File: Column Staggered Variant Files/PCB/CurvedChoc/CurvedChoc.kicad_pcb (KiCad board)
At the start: 2 copper layers, 118.9 x 178.7 mm, 54 parts, among them SW1 2-Pos, SW10 Switch, SW11 Switch, SW12 Switch, SW13 Switch, SW14 Switch, SW15 Switch, SW16 Switch, SW17 Switch, SW18 REsw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

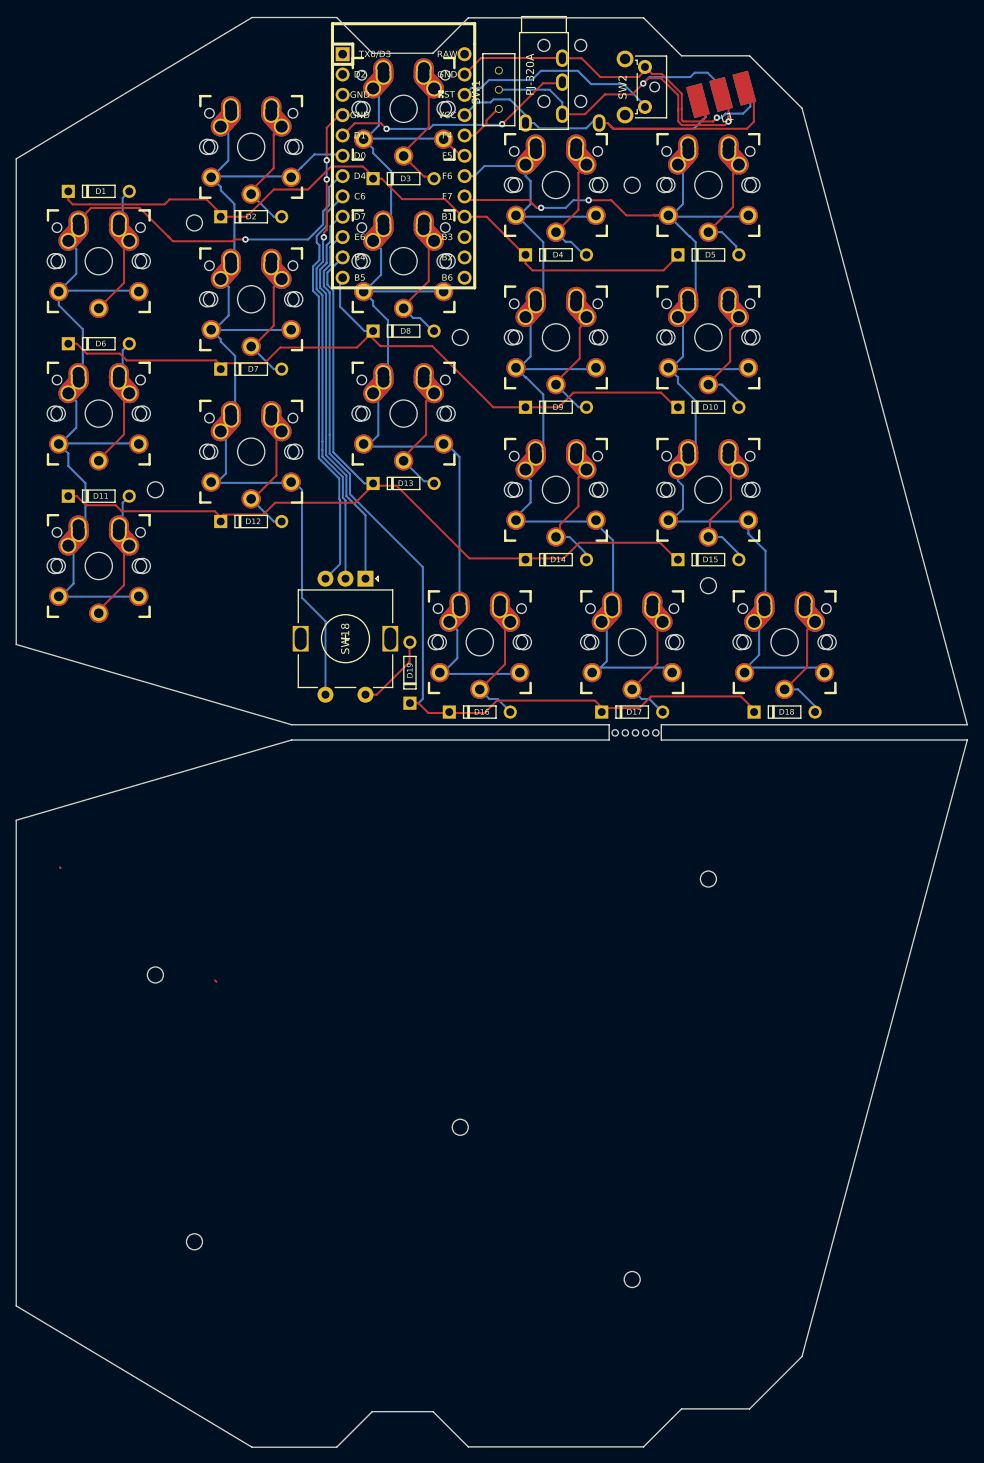
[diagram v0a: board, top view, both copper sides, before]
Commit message: Updated to include Rev2 QMK and Gerbers
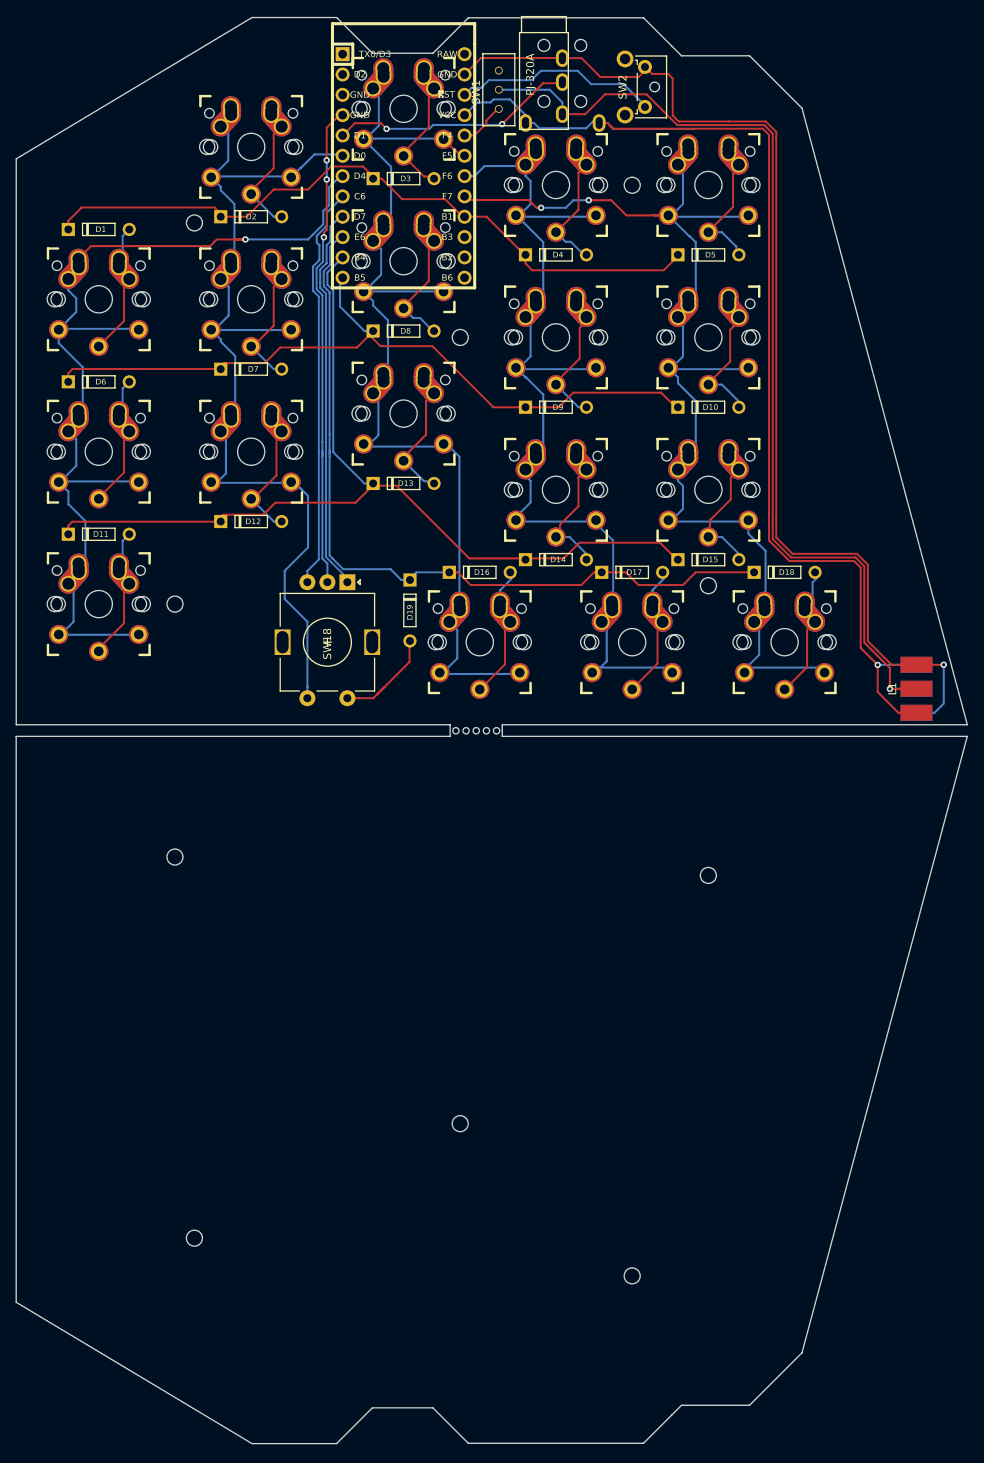
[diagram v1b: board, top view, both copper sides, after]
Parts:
- removed REF**: breakaway-mousebites, random-keyboard-parts:breakaway-mousebites
- added M1: MouseBite, KeyboardFootprints:Mousebite, F.Cu at (121.0, 105.8)
- moved L1 78.2 mm to (176.0, 100.3), turned to 270 degrees
- moved D16 17.5 mm to (121.4, 85.7)
- moved D17 17.5 mm to (140.5, 85.7)
- moved D18 17.5 mm to (159.5, 85.7)
- moved H1 14.9 mm to (83.3, 121.3)
- moved H1 14.5 mm to (83.3, 89.7)
- moved SW18 9.26 mm to (102.4, 94.5)
- moved D19 7.78 mm to (112.7, 90.5), turned to 270 degrees
- moved D11 4.76 mm to (73.8, 81.0)
- moved D6 4.76 mm to (73.8, 61.9)
- moved SW3 4.76 mm to (73.8, 51.6)
- moved SW8 4.76 mm to (73.8, 70.6)
- moved D1 4.76 mm to (73.8, 42.9)
- moved SW13 4.76 mm to (73.8, 89.7)
- moved H4 0.45 mm to (119.0, 154.6)
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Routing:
- net GND: track 48.8 -> 139.2 mm
- net VCC: track 58.2 -> 144.3 mm, vias 0 -> 1
- net DI: track 50.2 -> 125.9 mm, vias 2 -> 1
- net Row3: track 111.1 -> 98.2 mm
- net Col0: track 115.9 -> 120.9 mm
- net Net-(D19-Pad1): track 9.62 -> 13.4 mm
- net Col1: track 109.9 -> 112.0 mm
- net Net-(D16-Pad1): track 15.9 -> 14.2 mm
- net E2: track 51.8 -> 50.3 mm
- net Net-(D17-Pad1): track 15.3 -> 13.9 mm
- net E1: track 48.4 -> 47.4 mm
- net Net-(D18-Pad1): track 15.1 -> 14.3 mm
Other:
- board size 118.9 x 178.7 mm -> 118.9 x 178.3 mm
